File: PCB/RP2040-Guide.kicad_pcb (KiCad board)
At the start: 2 copper layers, 45.2 x 93.4 mm, 35 parts, among them J1 USB_C_Receptacle_USB2.0, J2 SWD, J3 Conn_01x11, J4 Conn_01x11, J5 Conn_01x11, SW1 SW_Push, U1 W25Q128JVS, U2 USBLC6-2SC6, U3 RP2040, U4 XC6206PxxxMR-Regulator_Linear, Y1 12MHz

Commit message: Edit formatting on readme/pcb/schematic
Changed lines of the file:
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@@
     (property "exclude_from_bom" "")
     (attr through_hole exclude_from_bom)
-    (fp_text reference "J3" (at 0 -2.77) (layer "F.SilkS")
+    (fp_text reference "J3" (at 0 -2.77) (layer "F.SilkS") hide
       (effects (font (size 1 1) (thickness 0.15)))
     )

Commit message: Update guide (Thanks xyz!)
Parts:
- added C7: 10uF, Capacitor_SMD:C_0402_1005Metric, B.Cu at (196.0, 50.0)
- R5, R6: footprint Resistor_SMD:R_0603_1608Metric -> Resistor_SMD:R_0402_1005Metric
- moved C17 3.00 mm to (196.0, 51.1), turned to 180 degrees
- moved R6 0.99 mm to (199.5, 56.5)
- moved R5 0.93 mm to (200.5, 56.5)
- renumbered C9 to C10, C10 to C11, C11 to C12, C12 to C13, C13 to C14, C14 to C15, C15 to C16, C16 to C17, C7 to C8, C8 to C9, R2 to R1, R1 to R2
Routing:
- net GND: track 59.2 -> 61.1 mm, vias 15 -> 16
- net +3V3: track 77.2 -> 75.7 mm
- net D_P: track 13.3 -> 14.4 mm
- net D_N: track 13.4 -> 14.5 mm
- net /D_-: track 7.54 -> 6.78 mm
- net /D_+: track 7.35 -> 6.66 mm

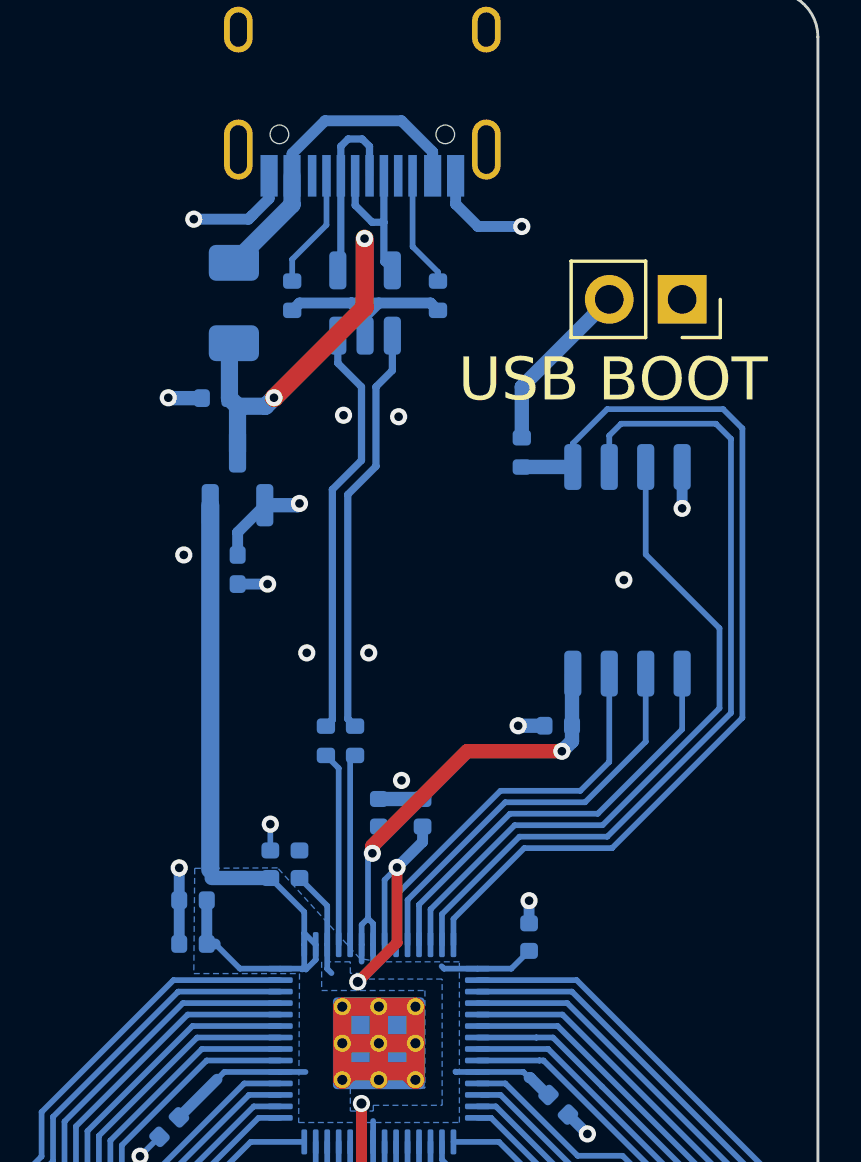
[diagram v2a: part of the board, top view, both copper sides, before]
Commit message: Update BOM and borked vias (Thanks to SpeedyPotato!)
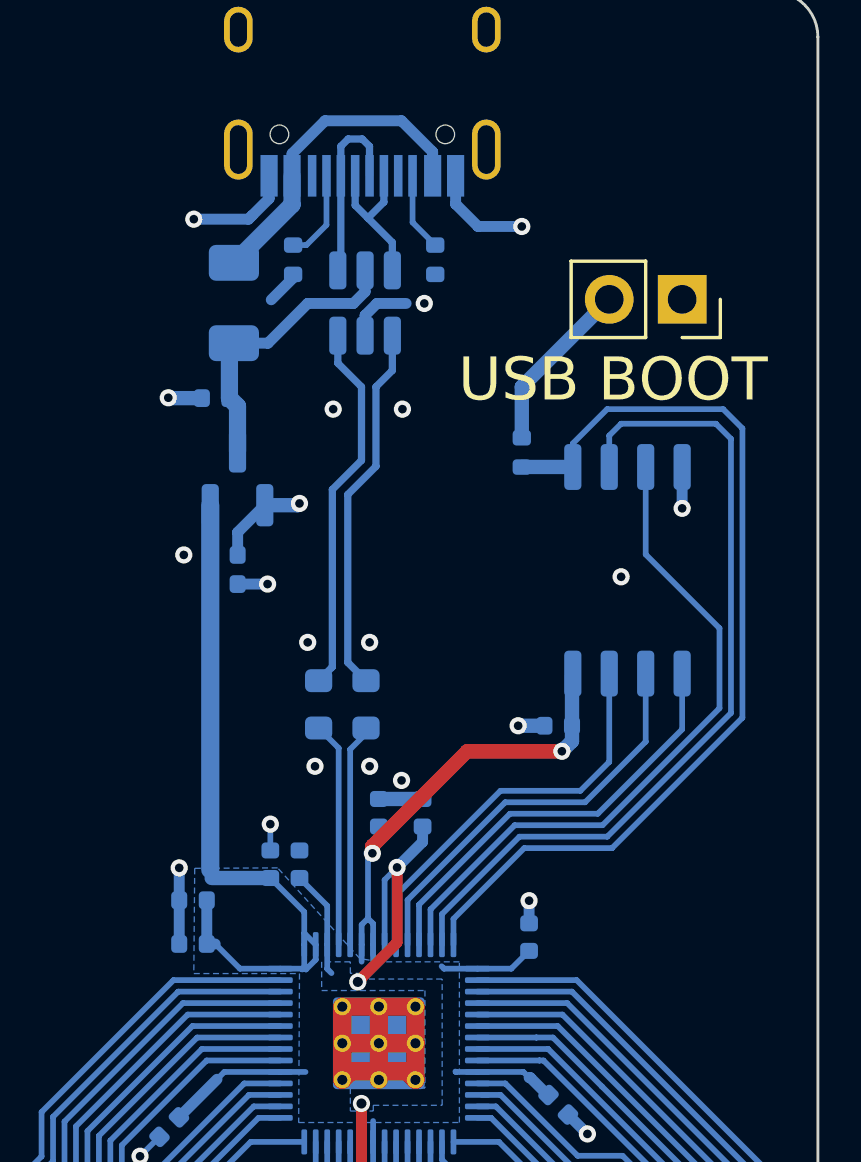
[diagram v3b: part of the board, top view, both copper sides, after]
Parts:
- R5, R6: footprint Resistor_SMD:R_0402_1005Metric -> Resistor_SMD:R_0603_1608Metric
- moved R5 1.33 mm to (200.9, 55.2)
- moved R6 1.30 mm to (199.3, 55.2)
- moved R4 1.26 mm to (203.3, 39.8)
- moved R3 1.25 mm to (198.4, 39.8)
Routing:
- net GND: track 61.1 -> 56.8 mm, vias 16 -> 24
- net +5V: track 13.1 -> 9.79 mm, vias 2 -> 0
- net D_N: track 14.5 -> 13.0 mm
- net D_P: track 14.4 -> 12.9 mm
- net /CC2: track 4.03 -> 2.74 mm
- net /D_+: track 6.66 -> 7.78 mm
- net /D_-: track 6.78 -> 7.84 mm
- net /CC1: track 4.16 -> 3.17 mm
- net (no net): vias 6 -> 1
- added copper zone on B.Cu, net +1V1
- removed copper zone on B.Cu, net (none)

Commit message: Update guide a bit
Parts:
- R2: value 10k -> 1k
- moved R2 0.39 mm to (193.8, 81.7)
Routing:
- net +3V3: track 75.7 -> 75.2 mm
- net GND: vias 24 -> 25
- net (no net): vias 1 -> 0
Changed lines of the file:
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@@
   )
   (footprint "Resistor_SMD:R_0402_1005Metric" (layer "B.Cu")
-    (at 193.51625 81.391125 180)
+    (at 193.802 81.661 180)
     (descr "Resistor SMD 0402 (1005 Metric), square (rectangular) end terminal, IPC_7351 nominal, (Body size source: IPC-SM-782 page 72, https://www.pcb-3d.com/wordpress/wp-content/uploads/ipc-sm-782a_amendment_1_and_2.pdf), generated with kicad-footprint-generator")
     (tags "resistor")
-    (property "LCSC" "C25744")
+    (property "LCSC" "C11702")
     (property "Sheetfile" "RP2040-Guide.kicad_sch")
     (property "Sheetname" "")
@@
       (effects (font (size 1 1) (thickness 0.15)) (justify mirror))
     )
-    (fp_text value "10k" (at 0 -1.17) (layer "B.Fab")
+    (fp_text value "1k" (at 0 -1.17) (layer "B.Fab")
       (effects (font (size 1 1) (thickness 0.15)) (justify mirror))
     )
@@
     (effects (font (size 1.6 1.6) (thickness 0.3)))
   )
-  (via (at 202.15225 57.896125) (size 0.6) (drill 0.3) (layers "F.Cu" "B.Cu") (free) (net 0))
   (segment (start 201.00925 73.263125) (end 195.929261 78.343114) (width 0.5) (layer "F.Cu") (net 1))
-  (segment (start 201.13625 60.182125) (end 204.43825 56.880125) (width 0.5) (layer "F.Cu") (net 1))
-  (segment (start 204.43825 56.880125) (end 207.74025 56.880125) (width 0.5) (layer "F.Cu") (net 1))
-  (segment (start 201.13625 60.436125) (end 201.13625 60.182125) (width 0.5) (layer "F.Cu") (net 1))
+  (segment (start 201.13625 60.436125) (end 204.69225 56.880125) (width 0.5) (layer "F.Cu") (net 1))
   (segment (start 195.929261 78.343114) (end 195.929261 78.343125) (width 0.5) (layer "F.Cu") (net 1))
+  (segment (start 204.69225 56.880125) (end 207.74025 56.880125) (width 0.5) (layer "F.Cu") (net 1))
   (segment (start 195.80225 78.470136) (end 195.80225 83.931125) (width 0.5) (layer "F.Cu") (net 1))
   (segment (start 195.929261 78.343125) (end 195.80225 78.470136) (width 0.5) (layer "F.Cu") (net 1))
@@
   (segment (start 201.162 70.493607) (end 201.162 69.764357) (width 0.2) (layer "B.Cu") (net 1))
   (segment (start 200.762 63.618607) (end 200.762 64.212357) (width 0.2) (layer "B.Cu") (net 1))
-  (segment (start 195.80225 83.167125) (end 194.02625 81.391125) (width 0.5) (layer "B.Cu") (net 1))
   (segment (start 206.59725 68.255607) (end 206.39775 68.056107) (width 0.2) (layer "B.Cu") (net 1))
   (segment (start 201.162 73.110375) (end 201.162 70.493607) (width 0.2) (layer "B.Cu") (net 1))
   (segment (start 200.98385 60.588525) (end 200.98385 62.703507) (width 0.2) (layer "B.Cu") (net 1))
   (segment (start 197.9245 64.456107) (end 198.79375 64.456107) (width 0.2) (layer "B.Cu") (net 1))
+  (segment (start 195.80225 83.15125) (end 194.312 81.661) (width 0.5) (layer "B.Cu") (net 1))
   (segment (start 198.762 63.618607) (end 198.762 62.478875) (width 0.2) (layer "B.Cu") (net 1))
   (segment (start 201.13625 60.436125) (end 201.13625 60.024107) (width 0.2) (layer "B.Cu") (net 1))
@@
   (segment (start 195.66 63.595357) (end 195.365 63.595357) (width 0.381) (layer "B.Cu") (net 1))
   (segment (start 201.00925 73.263125) (end 201.162 73.110375) (width 0.2) (layer "B.Cu") (net 1))
+  (segment (start 195.80225 83.931125) (end 195.80225 83.15125) (width 0.5) (layer "B.Cu") (net 1))
   (segment (start 201.13625 60.024107) (end 201.362 59.798357) (width 0.2) (layer "B.Cu") (net 1))
-  (segment (start 195.80225 83.931125) (end 195.80225 83.167125) (width 0.5) (layer "B.Cu") (net 1))
   (segment (start 197.9245 64.456107) (end 196.52075 64.456107) (width 0.2) (layer "B.Cu") (net 1))
   (segment (start 198.762 63.618607) (end 198.762 64.417357) (width 0.2) (layer "B.Cu") (net 1))
@@
   (via (at 211.93125 48.415125) (size 0.6) (drill 0.3) (layers "F.Cu" "B.Cu") (net 2))
   (via (at 202.946 41.275) (size 0.6) (drill 0.3) (layers "F.Cu" "B.Cu") (free) (net 2))
+  (via (at 202.15225 57.896125) (size 0.6) (drill 0.3) (layers "F.Cu" "B.Cu") (free) (net 2))
   (via (at 201.041 53.086) (size 0.6) (drill 0.3) (layers "F.Cu" "B.Cu") (free) (net 2))
   (via (at 207.077 77.073125) (size 0.6) (drill 0.3) (layers "F.Cu" "B.Cu") (net 2))
@@
   (segment (start 202.537 36.826875) (end 202.537 38.451) (width 0.2) (layer "B.Cu") (net 12))
   (segment (start 202.537 38.451) (end 203.327 39.241) (width 0.2) (layer "B.Cu") (net 12))
-  (segment (start 199.562 71.465381) (end 199.142736 71.884645) (width 0.2) (layer "B.Cu") (net 14))
-  (segment (start 191.55833 80.070205) (end 192.87925 81.391125) (width 0.2) (layer "B.Cu") (net 14))
-  (segment (start 191.55833 76.960081) (end 191.55833 80.070205) (width 0.2) (layer "B.Cu") (net 14))
-  (segment (start 199.562 70.493607) (end 199.562 71.465381) (width 0.2) (layer "B.Cu") (net 14))
-  (segment (start 196.633766 71.884645) (end 191.55833 76.960081) (width 0.2) (layer "B.Cu") (net 14))
-  (segment (start 193.26225 83.931125) (end 193.26225 81.647125) (width 0.2) (layer "B.Cu") (net 14))
-  (segment (start 193.26225 81.647125) (end 193.00625 81.391125) (width 0.2) (layer "B.Cu") (net 14))
-  (segment (start 199.142736 71.884645) (end 196.633766 71.884645) (width 0.2) (layer "B.Cu") (net 14))
+  (segment (start 193.26225 83.931125) (end 193.26225 81.69075) (width 0.2) (layer "B.Cu") (net 14))
+  (segment (start 191.55833 76.960081) (end 196.633766 71.884645) (width 0.2) (layer "B.Cu") (net 14))
+  (segment (start 193.26225 81.69075) (end 193.292 81.661) (width 0.2) (layer "B.Cu") (net 14))
+  (segment (start 191.55833 80.070205) (end 191.55833 76.960081) (width 0.2) (layer "B.Cu") (net 14))
+  (segment (start 196.633766 71.884645) (end 199.142736 71.884645) (width 0.2) (layer "B.Cu") (net 14))
+  (segment (start 193.292 81.661) (end 193.149125 81.661) (width 0.2) (layer "B.Cu") (net 14))
+  (segment (start 199.562 71.465381) (end 199.562 70.493607) (width 0.2) (layer "B.Cu") (net 14))
+  (segment (start 199.142736 71.884645) (end 199.562 71.465381) (width 0.2) (layer "B.Cu") (net 14))
+  (segment (start 193.149125 81.661) (end 191.55833 80.070205) (width 0.2) (layer "B.Cu") (net 14))
   (segment (start 199.962 71.630387) (end 199.308222 72.284165) (width 0.2) (layer "B.Cu") (net 15))
   (segment (start 196.528761 73.876608) (end 196.528761 78.047142) (width 0.2) (layer "B.Cu") (net 15))
